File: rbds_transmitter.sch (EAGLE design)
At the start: 21 parts, among them IC1 MAX1551, SW1 FSMSM, U3 ATMEGA168, X1 HD44780LCD-1602, Y1 16Mhz

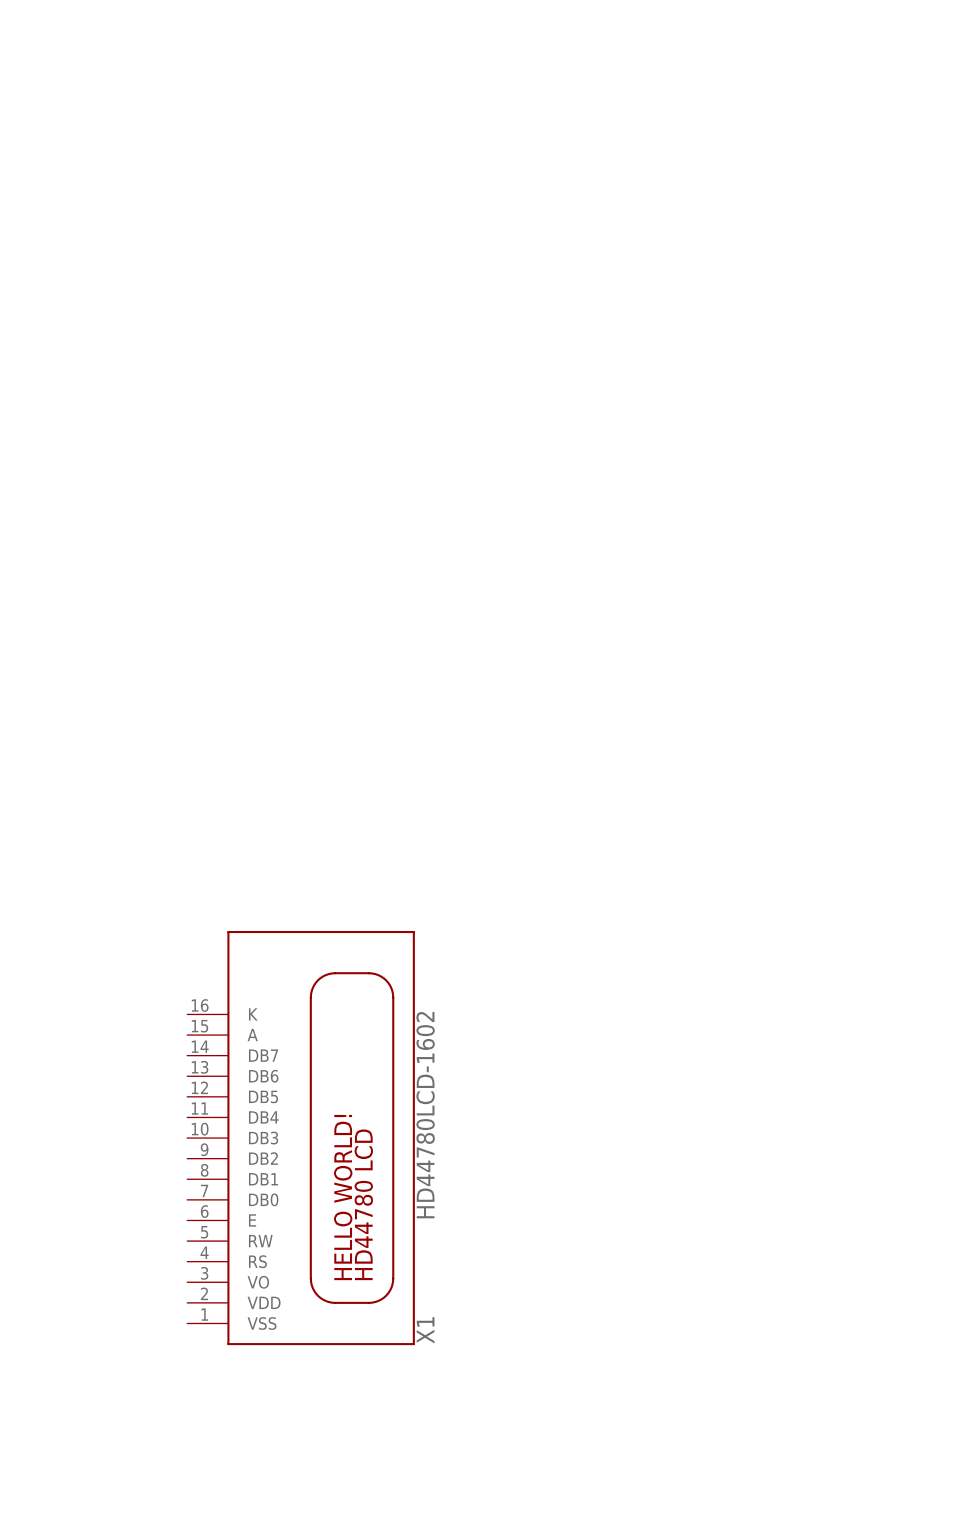
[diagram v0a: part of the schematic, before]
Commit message: added switching regulator
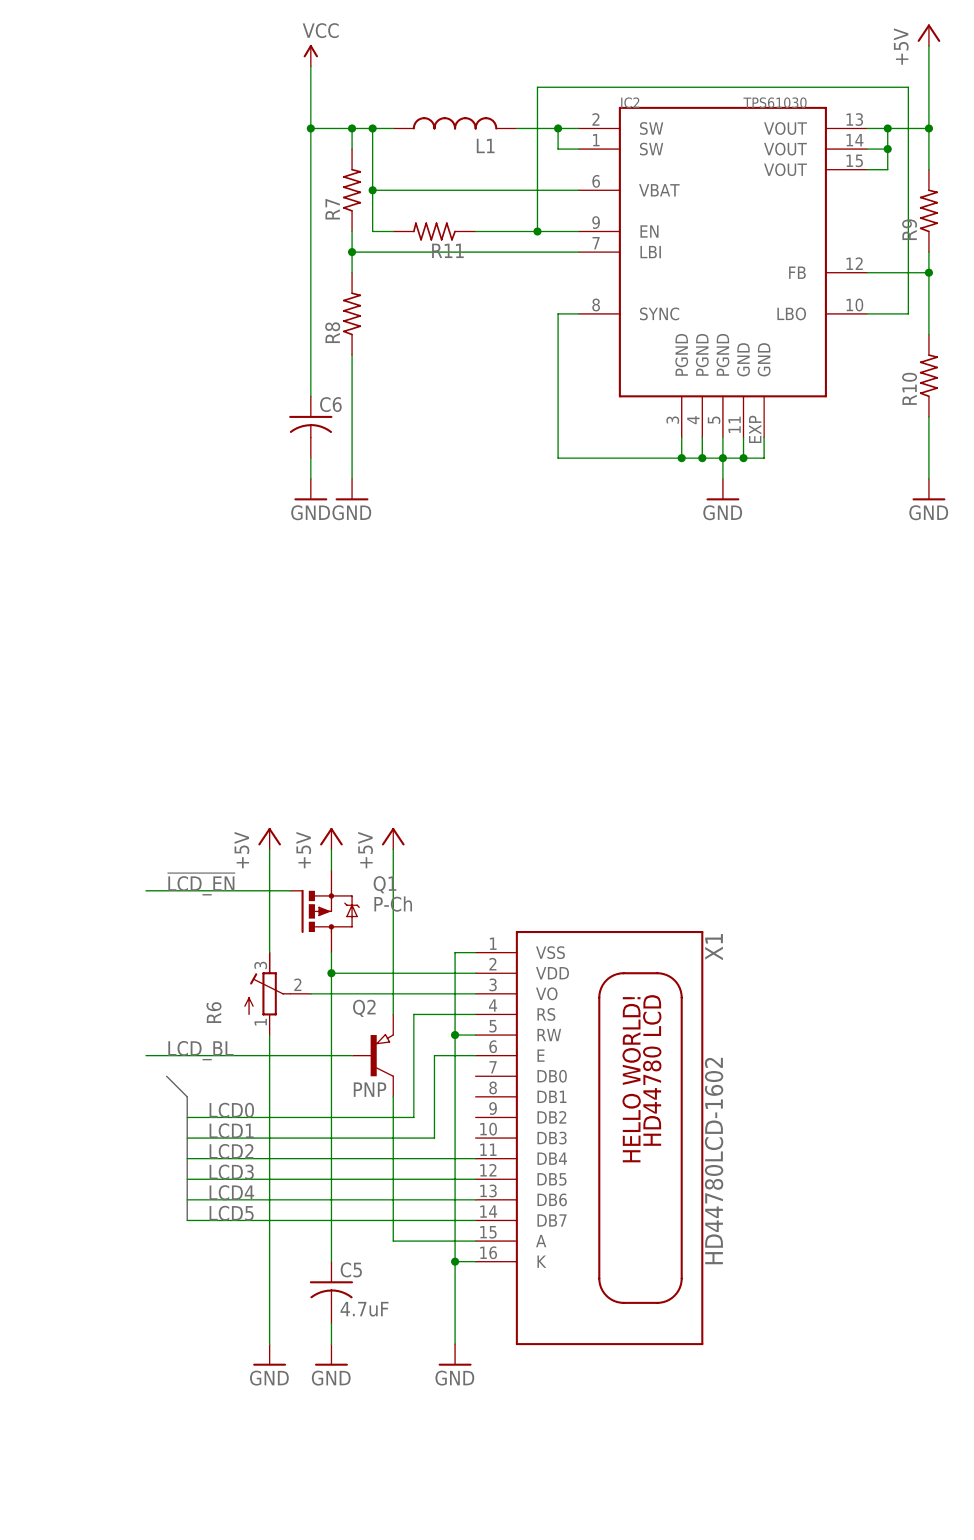
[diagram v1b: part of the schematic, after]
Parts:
- added C5: 4.7uF, adafruit:C-USC1206
- added C6: (no value), adafruit:C-USC1206
- added IC2: TPS61030, texas:TPS61030
- added L1: (no value), rcl:L-USL1812
- added Q1: P-Ch, transistor-power:IRLML5203
- added Q2: PNP, semicon-smd-ipc:PNP-TRANSISTOR_SOT23
- added R10, R11, R7, R8, R9: (no value), adafruit:R-US_R1206
- added R6: (no value), rcl:R-TRIMM4G/J
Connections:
- new net !LCD_EN: Q1.G
- new net LCD0: X1.RS
- new net LCD1: X1.E
- new net LCD2: X1.DB4
- new net LCD3: X1.DB5
- new net LCD4: X1.DB6
- new net LCD5: X1.DB7
- new net LCD_BL: Q2.B
- new net N$12: IC2.SW@0, IC2.SW@1, L1.2
- new net N$15: IC2.LBI, R7.1, R8.2
- new net N$16: IC2.EN, IC2.LBO, R11.1
- new net N$17: IC2.FB, R10.2, R9.1
- new net N$3: Q2.C, X1.A
- new net N$9: R6.S, X1.VO
- new net VDD: C5.1, Q1.D, X1.VDD
- net +5V: now also IC2.VOUT@0, IC2.VOUT@1, IC2.VOUT@2, Q1.S, Q2.E, R6.E, R9.2
- net GND: now also C5.2, C6.2, IC2.GND@0, IC2.GND@1, IC2.PGND@0, IC2.PGND@1, IC2.PGND@2, IC2.SYNC, R10.1, R6.A, R8.1, X1.K, X1.RW, X1.VSS
- net VCC: now also C6.1, IC2.VBAT, L1.1, R11.2, R7.2
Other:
- moved on the sheet: X1

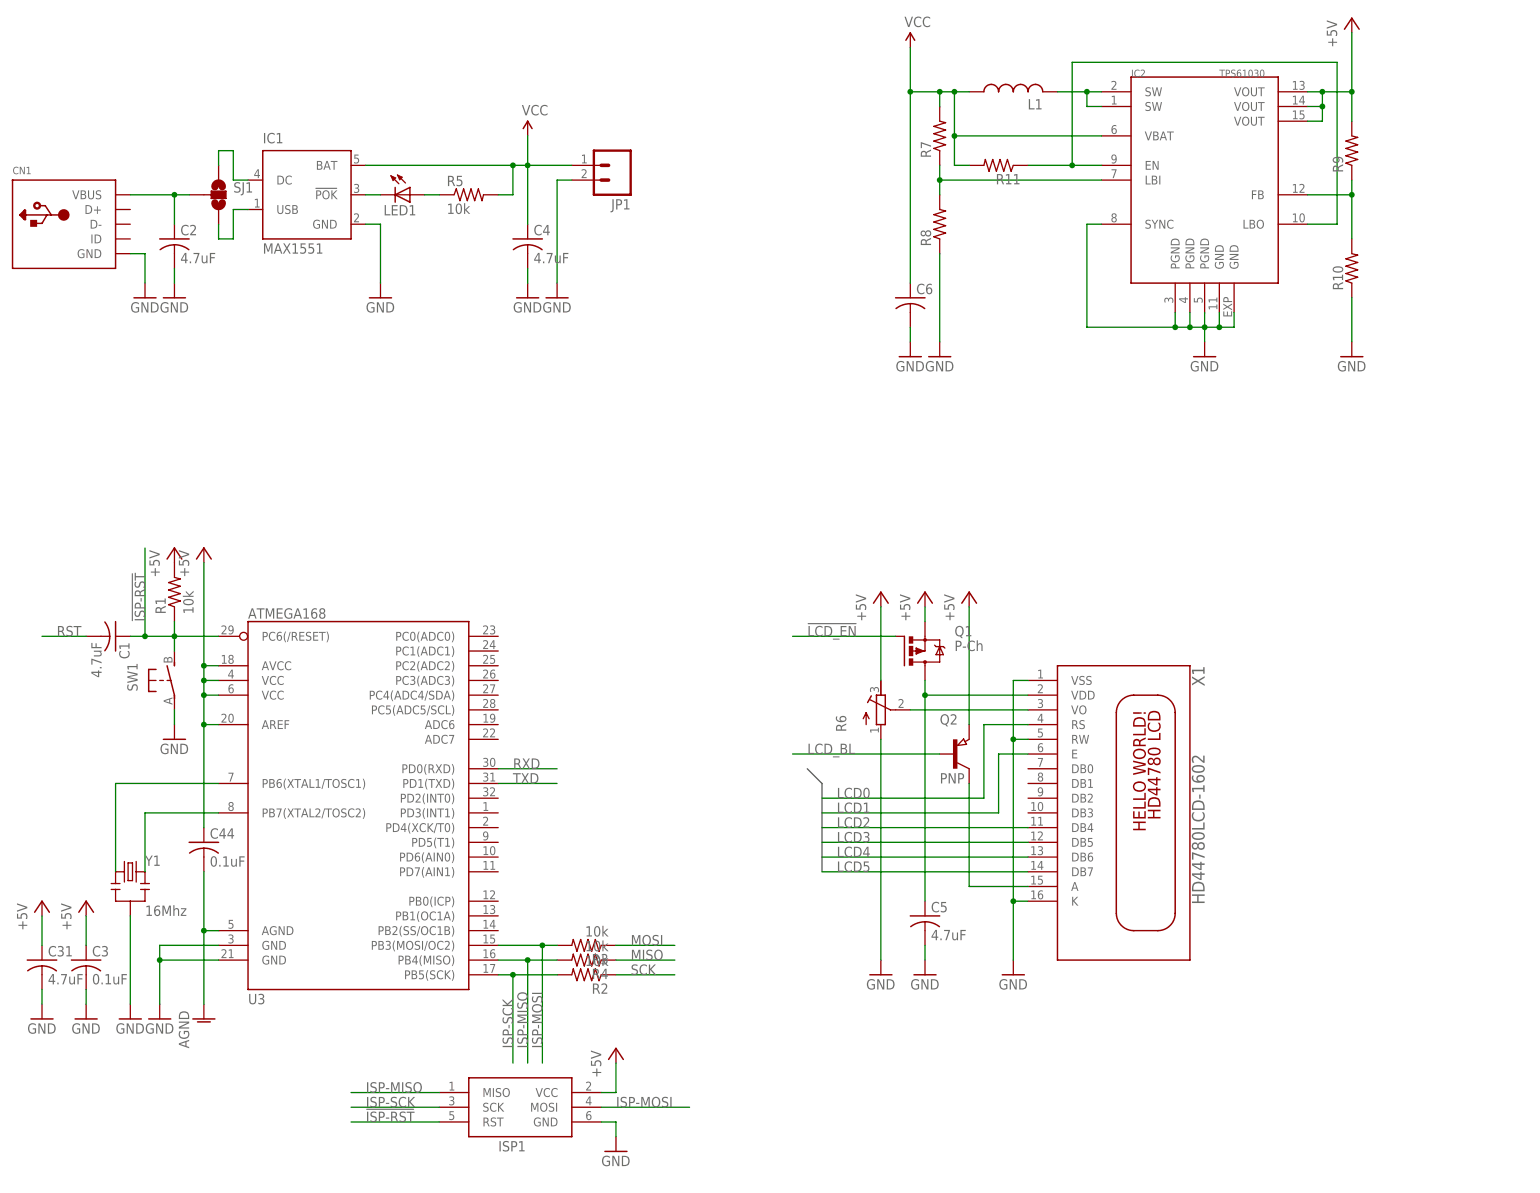
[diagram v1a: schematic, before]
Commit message: added dac, finished regulator
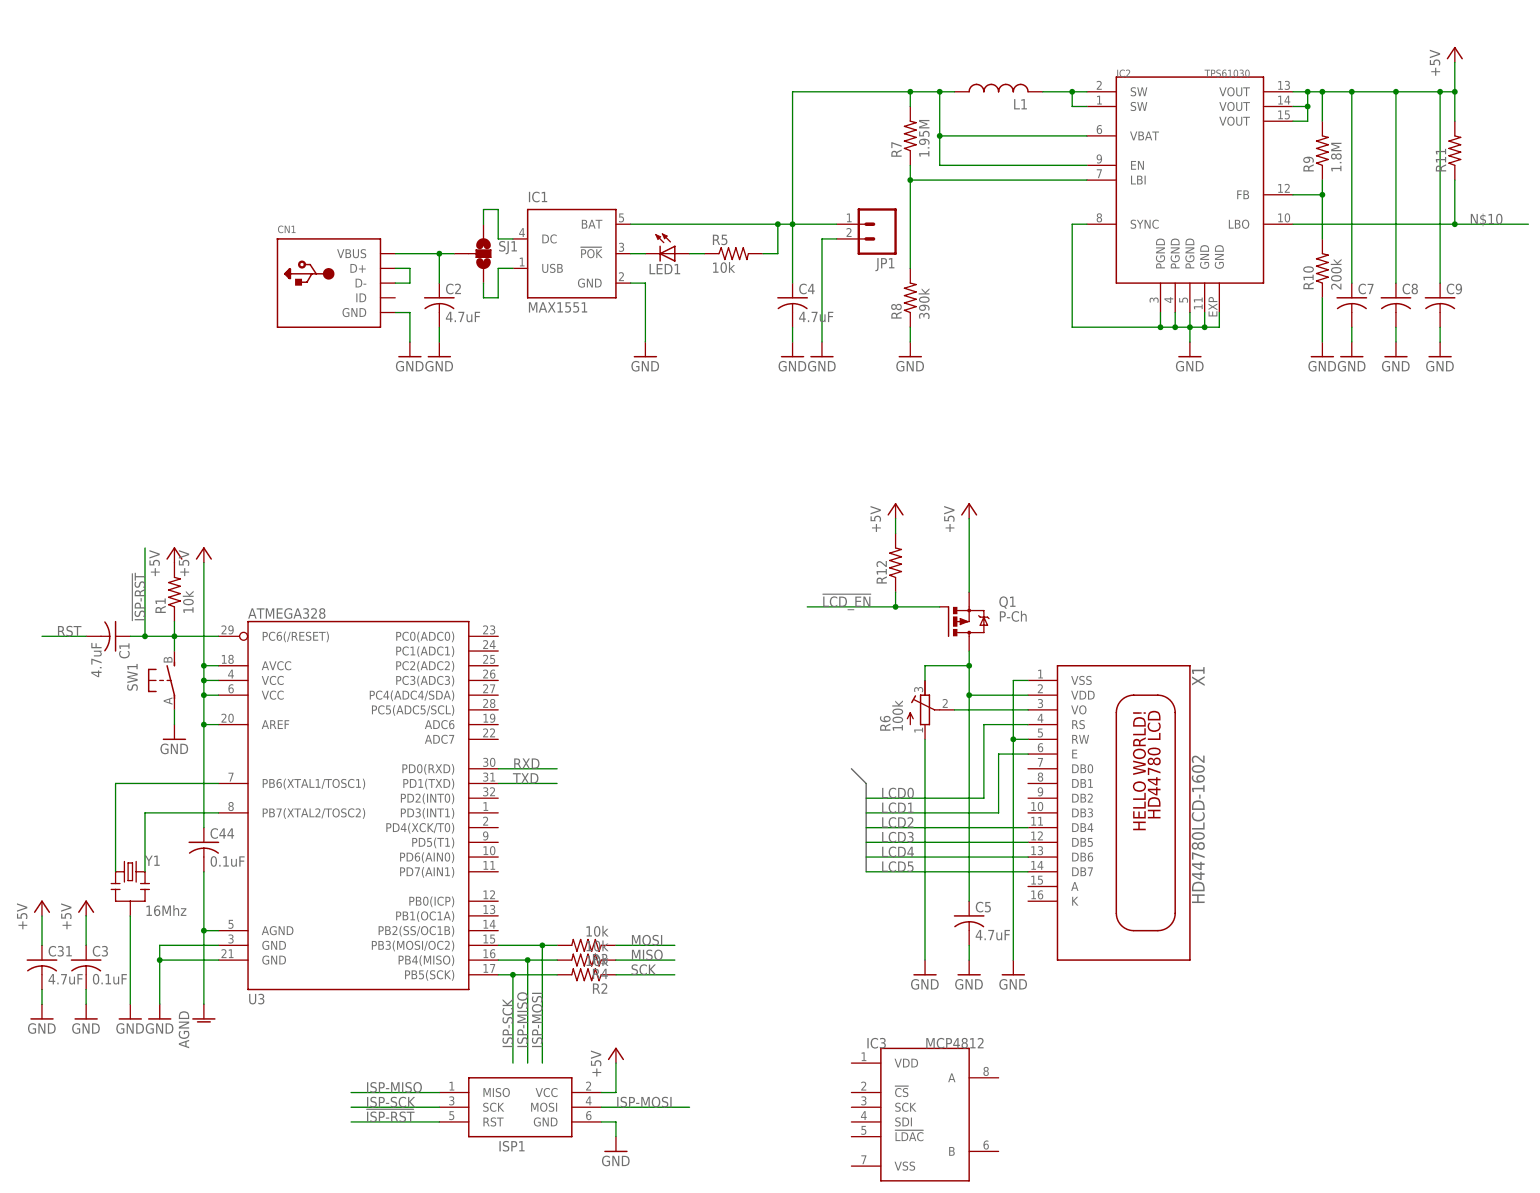
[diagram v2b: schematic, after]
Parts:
- removed C6: (no value), adafruit:C-USC1206
- removed Q2: PNP, semicon-smd-ipc:PNP-TRANSISTOR_SOT23
- added C7, C8, C9: (no value), adafruit:C-USC1206
- added IC3: MCP4812, microchip:MCP4812
- added R12: (no value), adafruit:R-US_R1206
- R10: value (none) -> 200k
- R6: value (none) -> 100k
- R7: value (none) -> 1.95M
- R8: value (none) -> 390k
- R9: value (none) -> 1.8M
- U3: value ATMEGA168 -> ATMEGA328
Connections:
- removed net LCD_BL: Q2.B
- removed net N$16: IC2.EN, IC2.LBO, R11.1
- removed net N$3: Q2.C, X1.A
- removed net VCC: C4.1, C6.1, IC1.BAT, IC2.VBAT, JP1.1, L1.1, R11.2, R5.2, R7.2
- new net N$10: IC2.LBO, R11.1
- new net N$11: C4.1, IC1.BAT, IC2.EN, IC2.VBAT, JP1.1, L1.1, R5.2, R7.2
- new net N$13: CN1.D+, CN1.D-
- net !LCD_EN: now also R12.1
- net +5V: now also C7.1, C8.1, C9.1, R11.2, R12.2; no longer Q2.E, R6.E
- net GND: now also C7.2, C8.2, C9.2; no longer C6.2, X1.K
- net VDD: now also R6.E
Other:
- moved on the sheet: C2, C4, C5, CN1, IC1, IC2, JP1, L1, LED1, Q1, R10, R11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
